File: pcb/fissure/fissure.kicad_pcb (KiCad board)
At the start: 2 copper layers, 127.5 x 95 mm, 117 parts, among them J1 AudioJack4, J2 AudioJack4, J3 Conn_01x04, J4 Conn_01x04, J5 Conn_01x03, J6 Conn_01x03, J7 Conn_01x04, J8 Conn_01x04, J9 Conn_01x04, K1 KEYSW, K10 KEYSW, K11 KEYSW, K12 KEYSW, K13 KEYSW, K14 KEYSW, K15 KEYSW, K16 KEYSW, K17 KEYSW, K18 KEYSW, K19 KEYSW, K2 KEYSW, K20 KEYSW, K3 KEYSW, K4 KEYSW, K5 KEYSW, K6 KEYSW, K7 KEYSW, K8 KEYSW, K9 KEYSW, SW1 SW_PUSH, U1 nice_nano, U2 MT25QL128ABA1ESE, U3 MT25QL128ABA1ESE

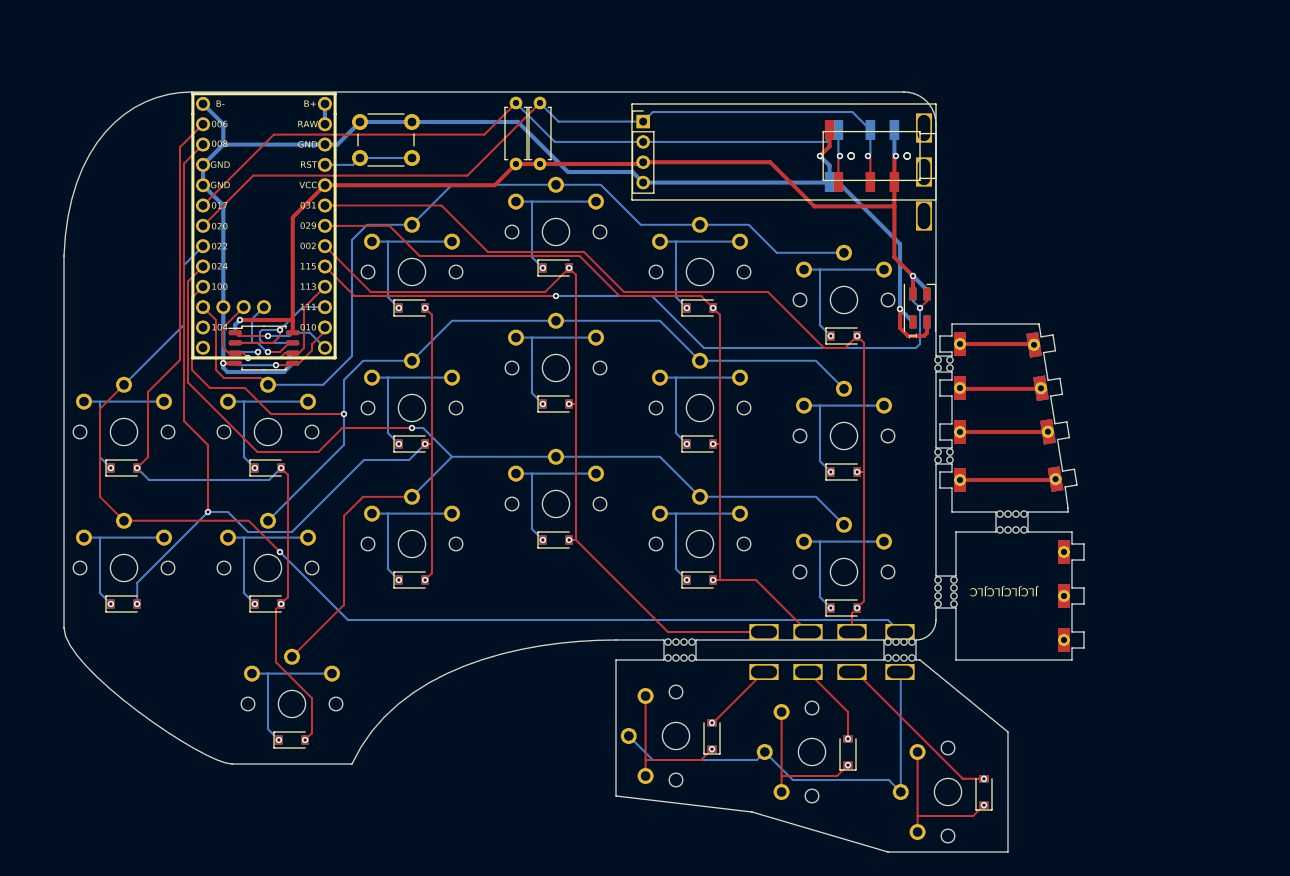
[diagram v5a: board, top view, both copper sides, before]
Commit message: Printed version (20 key steno + Qwerty) Y22
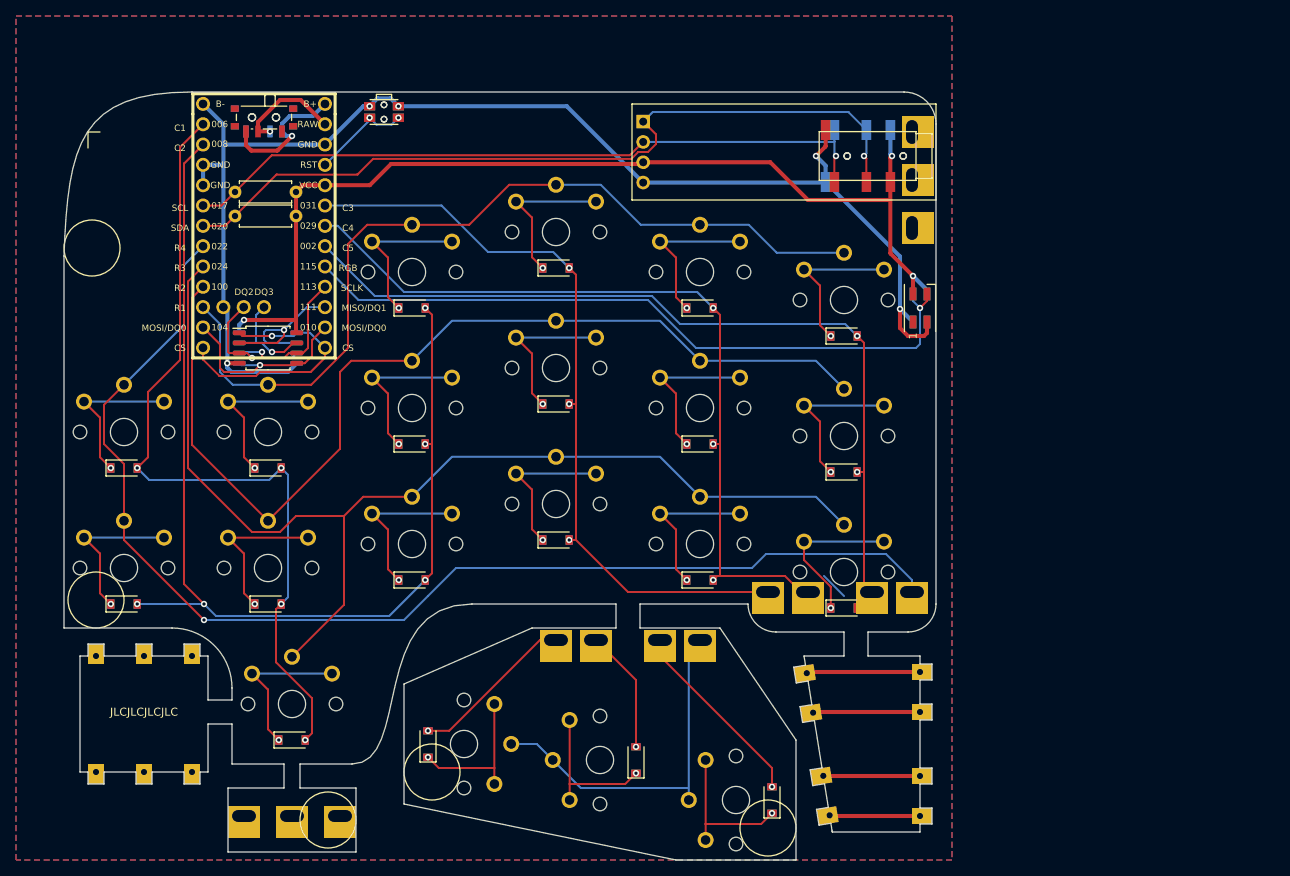
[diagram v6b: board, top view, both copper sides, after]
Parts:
- removed the J5 at (151.0, 108.0)
- removed REF** (x40): breakaway-hole-big, Keebio-Parts:breakaway-hole-big
- added J5: Conn_01x03, fissure:feet, F.Cu at (36.0, 130.0)
- added J5: Conn_01x03, fissure:feet, F.Cu at (36.0, 115.5)
- added J6: Conn_01x03, fissure:feet-conn, F.Cu at (54.5, 135.5)
- added SW2: SW_SPDT, Button_Switch_SMD:SW_SPDT_PCM12, B.Cu at (51.0, 48.5)
- added SW3: SW_SPDT, Button_Switch_SMD:SW_SPDT_PCM12, F.Cu at (51.0, 48.5)
- added SW4: SW_PUSH, Button_Switch_SMD:SW_SPST_EVQP7C, B.Cu at (66.0, 47.5)
- J3, J4, J7: moved to B.Cu
- SW1: footprint Button_Switch_THT:SW_PUSH_6mm -> Button_Switch_SMD:SW_SPST_EVQP7C
- moved J8 50.3 mm to (120.3, 126.5), turned to 99.1 degrees
- moved J7 41.8 mm to (133.0, 126.5), turned to 90 degrees
- moved D35 35.5 mm to (71.5, 126.5)
- moved D36 35.5 mm to (71.5, 126.5)
- moved R1 31.2 mm to (55.0, 60.5), turned to 180 degrees
- moved R2 27.7 mm to (55.0, 57.5), turned to 180 degrees
- moved D37 26.5 mm to (97.5, 128.5)
- moved D38 26.5 mm to (97.5, 128.5)
- moved D39 26.5 mm to (114.5, 133.5)
- moved D40 26.5 mm to (114.5, 133.5)
- moved K18 26.5 mm to (76.0, 126.5), turned to 90 degrees
- moved K19 26.5 mm to (93.0, 128.5)
- moved K20 26.5 mm to (110.0, 133.5)
- moved J4 25.3 mm to (96.5, 113.5)
- moved J3 5.22 mm to (123.0, 107.5)
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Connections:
- SW1 pad 1: GND -> RST
- SW1 pad 2: RST -> GND
- U1 pad 11: Net-(U1-Pad11) -> MOSI_DQ0
- U1 pad 12: Net-(U1-Pad12) -> CS
- U1 pad 18: COL3 -> COL5
- U1 pad 20: COL5 -> COL3
- U1 pad 24: RAW -> MCU_RAW
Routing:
- net CS: track 12.7 -> 31.6 mm
- net RAW: track 2.54 -> 17.4 mm, vias 0 -> 1
- net MCU_RAW: track 0.00 -> 13.4 mm, vias 0 -> 1
- net Net-(D35-Pad2): track 9.13 -> 20.7 mm
- net MOSI_DQ0: track 14.0 -> 25.4 mm
- net GND: track 164.7 -> 173.0 mm, vias 3 -> 5
- net ROW4: track 143.7 -> 151.8 mm
- net Net-(J4-Pad4): track 52.8 -> 45.0 mm
- net COL5: track 113.4 -> 106.3 mm, vias 3 -> 2
- net SCL: track 94.0 -> 88.9 mm
- net Net-(D37-Pad2): track 10.4 -> 15.4 mm
- net ROW3: track 144.0 -> 139.0 mm, vias 1 -> 0
- net Net-(D39-Pad2): track 22.0 -> 24.6 mm
- net ROW2: track 122.9 -> 125.3 mm, vias 1 -> 0
- net Net-(J7-Pad3): track 11.0 -> 13.4 mm
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- added copper zone on B.Cu, net GND
- added copper zone on F.Cu, net GND
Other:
- board size 127.5 x 95 mm -> 109 x 96 mm
- board text added: "C1"
- board text added: "C2"
- board text added: "C3"
- board text added: "C4"
- board text added: "C5"
- board text added: "CS"
- board text added: "DQ2"
- board text added: "DQ3"
- board text added: "MISO/DQ1"
- board text added: "MOSI/DQ0"
- board text added: "R1"
- board text added: "R2"
- board text added: "R3"
- board text added: "R4"
- board text added: "RGB"
- board text added: "SCL"
- board text added: "SCLK"
- board text added: "SDA"

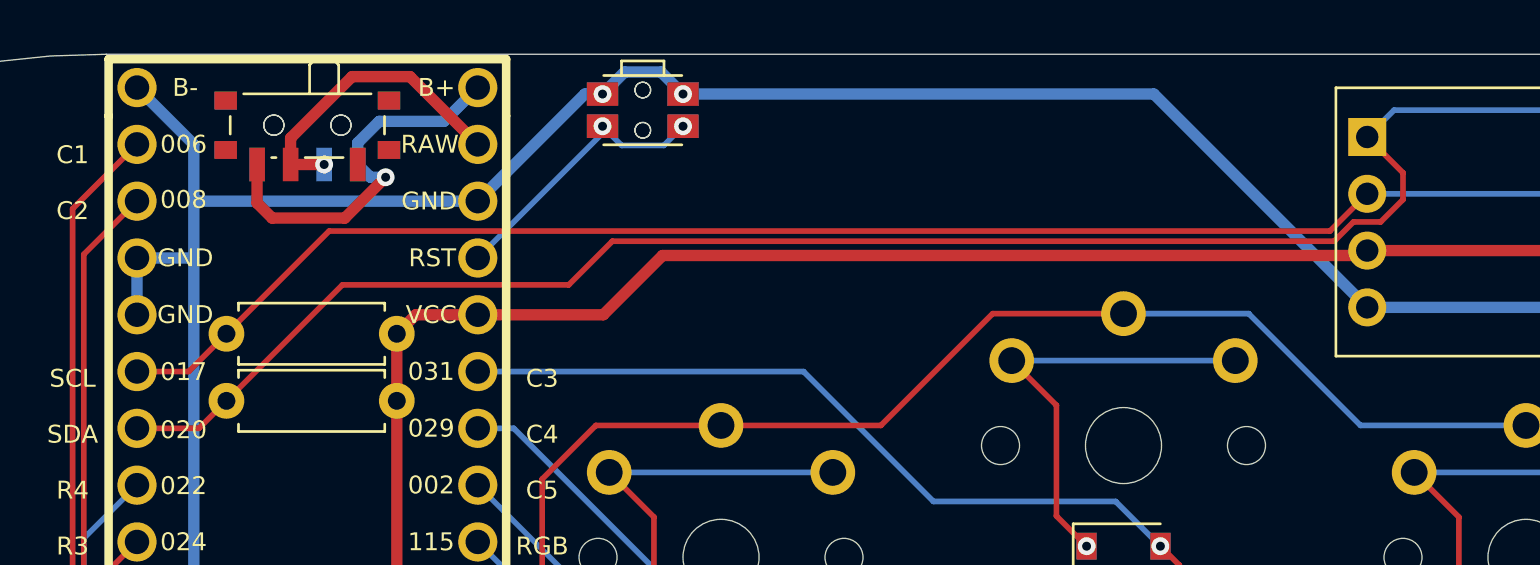
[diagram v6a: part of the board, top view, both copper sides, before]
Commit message: Correct SDA and SCL pins on promicro in schematics and board
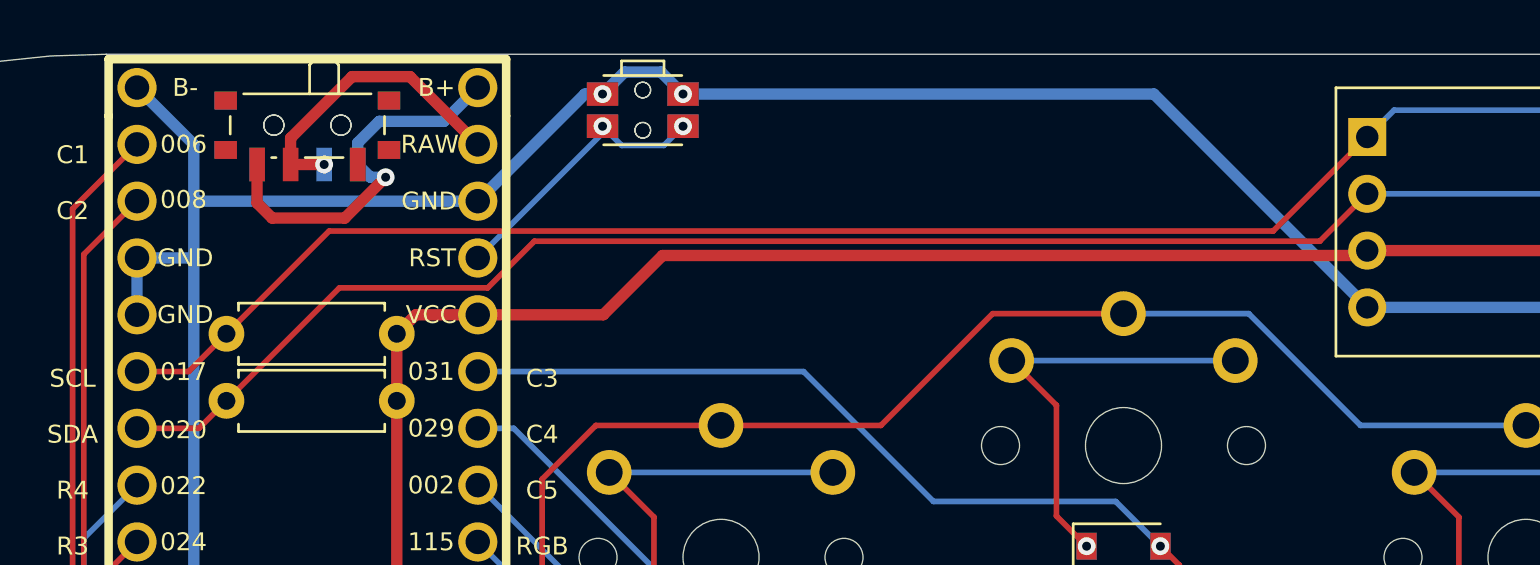
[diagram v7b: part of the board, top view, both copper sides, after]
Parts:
- removed the J5 at (36.0, 130.0)
- removed the J6 at (54.5, 135.5)
- added J10: Conn_01x03, fissure:feet, F.Cu at (36.0, 130.0)
- added J11: Conn_01x03, fissure:feet-conn, F.Cu at (54.5, 135.5)
- moved R1 3.00 mm to (55.0, 57.5)
- moved R2 3.00 mm to (55.0, 60.5)
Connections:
- U1 pad 5: SCL -> SDA
- U1 pad 6: SDA -> SCL
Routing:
- net SDA: track 100.4 -> 95.4 mm
- net SCL: track 88.9 -> 89.9 mm

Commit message: v3.1
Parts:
- removed J10: Conn_01x03, fissure:feet
- removed J11: Conn_01x03, fissure:feet-conn
- removed J7, J8: Conn_01x04, fissure:bridge
- removed the SW2 at (51.0, 48.5)
- removed SW3: SW_SPDT, Button_Switch_SMD:SW_SPDT_PCM12
- removed U3: MT25QL128ABA1ESE, Package_SO:SOP-8_5.28x5.23mm_P1.27mm
- added R3: R, Resistor_SMD:R_0805_2012Metric, B.Cu at (73.9, 88.1)
- added REF**: breakaway-mousebites, Keebio-Parts:breakaway-mousebites, F.Cu at (135.0, 93.0)
- added REF**: breakaway-mousebites, Keebio-Parts:breakaway-mousebites, F.Cu at (137.5, 93.0)
- added REF**: breakaway-mousebites, Keebio-Parts:breakaway-mousebites, F.Cu at (135.0, 70.0)
- added REF**: breakaway-mousebites, Keebio-Parts:breakaway-mousebites, F.Cu at (137.5, 70.0)
- added REF**: breakaway-mousebites, Keebio-Parts:breakaway-mousebites, F.Cu at (102.5, 108.8)
- added REF**: breakaway-mousebites, Keebio-Parts:breakaway-mousebites, F.Cu at (86.0, 108.8)
- added REF**: breakaway-mousebites, Keebio-Parts:breakaway-mousebites, F.Cu at (102.5, 112.0)
- added REF**: breakaway-mousebites, Keebio-Parts:breakaway-mousebites, F.Cu at (86.0, 112.0)
- D35, D37, D39, K18, K19, K20, U2: moved to B.Cu
- D36, D38, D40: moved to F.Cu
- J3: value Conn_01x04 -> Conn_01x08; moved to F.Cu
- J4: value Conn_01x04 -> Conn_01x08; footprint fissure:bridge-conn -> fissure:bridge; moved to F.Cu
- J5: value Conn_01x03 -> Conn_01x08; footprint fissure:feet -> fissure:bridge-conn; moved to B.Cu
- J6: value Conn_01x03 -> Conn_01x08; footprint fissure:feet-conn -> fissure:bridge
- R1, R2: footprint Resistor_THT:R_Axial_DIN0207_L6.3mm_D2.5mm_P7.62mm_Horizontal -> Resistor_SMD:R_0805_2012Metric; moved to B.Cu
- SW1: footprint Button_Switch_SMD:SW_SPST_EVQP7C -> Button_Switch_SMD:SW_SPST_EVQQ2
- SW2: renamed from SW4; footprint Button_Switch_SMD:SW_SPST_EVQP7C -> Button_Switch_SMD:SW_SPST_EVQQ2
- U1: value nice_nano -> ProMicro; footprint nice-nano-kicad:nice_nano -> Keebio-Parts:ArduinoProMicro
- moved J5 110.2 mm to (142.0, 85.5), turned to 90 degrees
- moved D35 102.9 mm to (174.2, 121.5)
- moved D36 102.9 mm to (174.2, 121.5)
- moved K18 93.9 mm to (169.8, 121.5)
- moved J1 90.0 mm to (73.0, 120.5), turned to 90 degrees
- moved J2 90.0 mm to (73.0, 120.5), turned to 270 degrees
- moved J9 85.7 mm to (126.5, 127.0), turned to 180 degrees
- moved R1 73.5 mm to (80.4, 126.5), turned to 0 degrees
- moved R2 72.6 mm to (80.4, 128.5), turned to 0 degrees
- moved J6 64.9 mm to (101.0, 113.0), turned to 180 degrees
- moved K19 60.2 mm to (153.0, 123.5)
- moved SW1 56.0 mm to (120.9, 58.6)
- moved SW2 56.0 mm to (120.9, 58.6)
- moved D37 51.2 mm to (148.5, 123.5)
- moved D38 51.2 mm to (148.5, 123.5)
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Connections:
- D35 pad 2: Net-(D35-Pad2) -> thumb_COL3
- D36 pad 2: Net-(D35-Pad2) -> thumb_COL3
- D37 pad 2: Net-(D37-Pad2) -> thumb_COL4
- D38 pad 2: Net-(D37-Pad2) -> thumb_COL4
- D39 pad 2: Net-(D39-Pad2) -> thumb_COL5
- D40 pad 2: Net-(D39-Pad2) -> thumb_COL5
- J1 pad R1: SDA -> bridge_SDA
- J1 pad R2: VCC -> bridge_VCC
- J1 pad S: GND -> bridge_GND
- J1 pad T: SCL -> bridge_SCL
- J2 pad R1: SDA -> bridge_SDA
- J2 pad R2: VCC -> bridge_VCC
- J2 pad S: GND -> bridge_GND
- J2 pad T: SCL -> bridge_SCL
- J4 pad 1: Net-(D35-Pad2) -> Net-(J4-Pad1)
- J4 pad 2: Net-(D37-Pad2) -> Net-(J4-Pad2)
- J4 pad 3: Net-(D39-Pad2) -> Net-(J4-Pad3)
- J5 pad 1: Net-(J5-Pad1) -> thumb_COL3
- J5 pad 2: Net-(J5-Pad2) -> thumb_COL4
- J5 pad 3: Net-(J5-Pad3) -> thumb_COL5
- J6 pad 1: Net-(J6-Pad1) -> Net-(J4-Pad1)
- J6 pad 2: Net-(J6-Pad2) -> Net-(J4-Pad2)
- J6 pad 3: Net-(J6-Pad3) -> Net-(J4-Pad3)
- J9 pad 1: SDA -> bridge_GND
- J9 pad 2: SCL -> bridge_VCC
- J9 pad 3: VCC -> bridge_SCL
- J9 pad 4: GND -> bridge_SDA
- K18 pad 1: Net-(J4-Pad4) -> thumb_ROW4
- K19 pad 1: Net-(J4-Pad4) -> thumb_ROW4
- K20 pad 1: Net-(J4-Pad4) -> thumb_ROW4
- R1 pad 1: VCC -> bridge_VCC
- R1 pad 2: SDA -> bridge_SDA
- R2 pad 1: VCC -> bridge_VCC
- R2 pad 2: SCL -> bridge_SCL
- U1 pad 11: MOSI_DQ0 -> ROW2
- U1 pad 12: CS -> ROW3
- U1 pad 24: MCU_RAW -> RAW
- U1 pad 7: ROW4 -> Net-(U1-Pad7)
- U1 pad 8: ROW3 -> Net-(U1-Pad8)
- U1 pad 9: ROW2 -> ROW4
- U2 pad 3: DQ2 -> Net-(R3-Pad2)
- U2 pad 7: DQ3 -> Net-(R3-Pad2)
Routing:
- net thumb_ROW4: track 0.00 -> 73.1 mm
- net bridge_VCC: track 0.00 -> 72.9 mm, vias 0 -> 2
- net bridge_SDA: track 0.00 -> 62.9 mm, vias 0 -> 2
- net bridge_GND: track 0.00 -> 62.2 mm, vias 0 -> 1
- net bridge_SCL: track 0.00 -> 61.7 mm, vias 0 -> 1
- net RST: track 12.5 -> 57.2 mm, vias 2 -> 1
- net COL2: track 133.5 -> 91.9 mm, vias 5 -> 4
- net thumb_COL5: track 0.00 -> 38.4 mm, vias 0 -> 1
- net thumb_COL3: track 0.00 -> 36.5 mm, vias 0 -> 1
- net ROW2: track 125.3 -> 90.8 mm, vias 0 -> 1
- net Net-(J4-Pad3): track 0.00 -> 34.0 mm
- net thumb_COL4: track 0.00 -> 29.9 mm, vias 0 -> 1
- net CS: track 31.6 -> 3.68 mm, vias 1 -> 0
- net Net-(J4-Pad2): track 0.00 -> 27.6 mm
- net ROW4: track 151.8 -> 124.8 mm, vias 1 -> 0
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- removed copper zone on B.Cu, net GND
- removed copper zone on F.Cu, net GND
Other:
- board size 109 x 96 mm -> 151.2 x 81.6 mm
- rule pad_to_mask_clearance: 0.051 -> 0
- board text added: "4.7k"
- board text removed: "C1"
- board text removed: "C2"
- board text removed: "C3"
- board text removed: "C4"
- board text removed: "C5"
- board text removed: "CS"
- board text removed: "DQ2"
- board text removed: "DQ3"
- board text removed: "MISO/DQ1"
- board text removed: "MOSI/DQ0"
- board text removed: "R1"
- board text removed: "R2"
- board text removed: "R3"
- board text removed: "R4"
- board text removed: "RGB"
- board text removed: "SCL"
- board text removed: "SCLK"
- board text removed: "SDA"
